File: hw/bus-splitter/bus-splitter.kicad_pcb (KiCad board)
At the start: 2 copper layers, 93 x 22 mm, 29 parts, among them J1 WAGO 243-723, J2 WAGO 243-724, J3 WAGO 243-721, J4 WAGO 243-722, J5 CONN-ISP-6, J6 WAGO 243-723, J7 WAGO 243-724, J8 WAGO 243-721, J9 WAGO 243-722, U1 AM1S-2405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

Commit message: Feat: Finished PCB for review
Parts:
- added LOGO1: OPEN_HARDWARE_1, Symbol:Symbol_OSHW-Logo_Copper, F.Cu at (127.0, 88.0)
- D2: value D -> 1N4148
- F1: value FUSE -> 0,15A
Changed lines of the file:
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@@
     (tracks 156)
     (zones 0)
-    (modules 29)
+    (modules 30)
     (nets 21)
   )
@@
   (title_block
     (title bus-splitter)
-    (date 2018-06-13)
+    (date 2018-06-14)
     (rev 1)
     (company koewiba)
@@
       (effects (font (size 0.8 0.8) (thickness 0.15)) (justify mirror))
     )
-    (fp_text value D (at 0 -1.524 90) (layer B.Fab)
+    (fp_text value 1N4148 (at 0 -1.524 90) (layer B.Fab)
       (effects (font (size 0.8 0.8) (thickness 0.15)) (justify mirror))
     )
@@
       (effects (font (size 0.8 0.8) (thickness 0.15)) (justify mirror))
     )
-    (fp_text value FUSE (at -0.127 -1.905 90) (layer B.Fab)
+    (fp_text value 0,15A (at -0.127 -1.905 90) (layer B.Fab)
       (effects (font (size 0.8 0.8) (thickness 0.15)) (justify mirror))
     )
@@
     )
   )
+  (module Symbol:Symbol_OSHW-Logo_Copper (layer F.Cu)
+    (at 127 88)
+    (descr "Symbol, OSHW-Logo, Copper,")
+    (tags "Symbol, OSHW-Logo, Copper,")
+    (fp_text reference LOGO1 (at 0.09906 -4.38912) (layer F.SilkS) hide
+      (effects (font (size 1 1) (thickness 0.2)))
+    )
+    (fp_text value OPEN_HARDWARE_1 (at 0.30988 6.56082) (layer F.Fab) hide
+      (effects (font (size 1 1) (thickness 0.2)))
+    )
+    (fp_line (start 1.66878 2.68986) (end 2.02946 4.16052) (layer F.Cu) (width 0.381))
+    (fp_line (start 2.02946 4.16052) (end 2.30886 3.0988) (layer F.Cu) (width 0.381))
+    (fp_line (start 2.30886 3.0988) (end 2.61874 4.17068) (layer F.Cu) (width 0.381))
+    (fp_line (start 2.61874 4.17068) (end 2.9591 2.72034) (layer F.Cu) (width 0.381))
+    (fp_line (start 0.24892 3.38074) (end 1.03886 3.37058) (layer F.Cu) (width 0.381))
+    (fp_line (start 1.03886 3.37058) (end 1.04902 3.38074) (layer F.Cu) (width 0.381))
+    (fp_line (start 1.04902 3.38074) (end 1.04902 3.37058) (layer F.Cu) (width 0.381))
+    (fp_line (start 1.08966 2.65938) (end 1.08966 4.20116) (layer F.Cu) (width 0.381))
+    (fp_line (start 0.20066 2.64922) (end 0.20066 4.21894) (layer F.Cu) (width 0.381))
+    (fp_line (start 0.20066 4.21894) (end 0.21082 4.20878) (layer F.Cu) (width 0.381))
+    (fp_line (start -0.35052 2.75082) (end -0.70104 2.66954) (layer F.Cu) (width 0.381))
+    (fp_line (start -0.70104 2.66954) (end -1.02108 2.65938) (layer F.Cu) (width 0.381))
+    (fp_line (start -1.02108 2.65938) (end -1.25984 2.86004) (layer F.Cu) (width 0.381))
+    (fp_line (start -1.25984 2.86004) (end -1.29032 3.12928) (layer F.Cu) (width 0.381))
+    (fp_line (start -1.29032 3.12928) (end -1.04902 3.37058) (layer F.Cu) (width 0.381))
+    (fp_line (start -1.04902 3.37058) (end -0.6604 3.50012) (layer F.Cu) (width 0.381))
+    (fp_line (start -0.6604 3.50012) (end -0.48006 3.66014) (layer F.Cu) (width 0.381))
+    (fp_line (start -0.48006 3.66014) (end -0.43942 3.95986) (layer F.Cu) (width 0.381))
+    (fp_line (start -0.43942 3.95986) (end -0.67056 4.18084) (layer F.Cu) (width 0.381))
+    (fp_line (start -0.67056 4.18084) (end -0.9906 4.20878) (layer F.Cu) (width 0.381))
+    (fp_line (start -0.9906 4.20878) (end -1.34112 4.09956) (layer F.Cu) (width 0.381))
+    (fp_line (start -2.37998 2.64922) (end -2.6289 2.66954) (layer F.Cu) (width 0.381))
+    (fp_line (start -2.6289 2.66954) (end -2.8702 2.91084) (layer F.Cu) (width 0.381))
+    (fp_line (start -2.8702 2.91084) (end -2.9591 3.40106) (layer F.Cu) (width 0.381))
+    (fp_line (start -2.9591 3.40106) (end -2.93116 3.74904) (layer F.Cu) (width 0.381))
+    (fp_line (start -2.93116 3.74904) (end -2.7305 4.06908) (layer F.Cu) (width 0.381))
+    (fp_line (start -2.7305 4.06908) (end -2.47904 4.191) (layer F.Cu) (width 0.381))
+    (fp_line (start -2.47904 4.191) (end -2.16916 4.11988) (layer F.Cu) (width 0.381))
+    (fp_line (start -2.16916 4.11988) (end -1.95072 3.93954) (layer F.Cu) (width 0.381))
+    (fp_line (start -1.95072 3.93954) (end -1.8796 3.4798) (layer F.Cu) (width 0.381))
+    (fp_line (start -1.8796 3.4798) (end -1.9304 3.07086) (layer F.Cu) (width 0.381))
+    (fp_line (start -1.9304 3.07086) (end -2.03962 2.78892) (layer F.Cu) (width 0.381))
+    (fp_line (start -2.03962 2.78892) (end -2.4003 2.65938) (layer F.Cu) (width 0.381))
+    (fp_line (start -1.78054 0.92964) (end -2.03962 1.49098) (layer F.Cu) (width 0.381))
+    (fp_line (start -2.03962 1.49098) (end -1.50114 2.00914) (layer F.Cu) (width 0.381))
+    (fp_line (start -1.50114 2.00914) (end -0.98044 1.7399) (layer F.Cu) (width 0.381))
+    (fp_line (start -0.98044 1.7399) (end -0.70104 1.89992) (layer F.Cu) (width 0.381))
+    (fp_line (start 0.73914 1.8796) (end 1.06934 1.6891) (layer F.Cu) (width 0.381))
+    (fp_line (start 1.06934 1.6891) (end 1.50876 2.0193) (layer F.Cu) (width 0.381))
+    (fp_line (start 1.50876 2.0193) (end 1.9812 1.52908) (layer F.Cu) (width 0.381))
+    (fp_line (start 1.9812 1.52908) (end 1.69926 1.04902) (layer F.Cu) (width 0.381))
+    (fp_line (start 1.69926 1.04902) (end 1.88976 0.57912) (layer F.Cu) (width 0.381))
+    (fp_line (start 1.88976 0.57912) (end 2.49936 0.39116) (layer F.Cu) (width 0.381))
+    (fp_line (start 2.49936 0.39116) (end 2.49936 -0.28956) (layer F.Cu) (width 0.381))
+    (fp_line (start 2.49936 -0.28956) (end 1.94056 -0.42926) (layer F.Cu) (width 0.381))
+    (fp_line (start 1.94056 -0.42926) (end 1.7399 -1.00076) (layer F.Cu) (width 0.381))
+    (fp_line (start 1.7399 -1.00076) (end 2.00914 -1.47066) (layer F.Cu) (width 0.381))
+    (fp_line (start 2.00914 -1.47066) (end 1.53924 -1.9812) (layer F.Cu) (width 0.381))
+    (fp_line (start 1.53924 -1.9812) (end 1.02108 -1.71958) (layer F.Cu) (width 0.381))
+    (fp_line (start 1.02108 -1.71958) (end 0.55118 -1.92024) (layer F.Cu) (width 0.381))
+    (fp_line (start 0.55118 -1.92024) (end 0.381 -2.46126) (layer F.Cu) (width 0.381))
+    (fp_line (start 0.381 -2.46126) (end -0.30988 -2.47904) (layer F.Cu) (width 0.381))
+    (fp_line (start -0.30988 -2.47904) (end -0.5207 -1.9304) (layer F.Cu) (width 0.381))
+    (fp_line (start -0.5207 -1.9304) (end -0.9398 -1.76022) (layer F.Cu) (width 0.381))
+    (fp_line (start -0.9398 -1.76022) (end -1.49098 -2.02946) (layer F.Cu) (width 0.381))
+    (fp_line (start -1.49098 -2.02946) (end -2.00914 -1.50114) (layer F.Cu) (width 0.381))
+    (fp_line (start -2.00914 -1.50114) (end -1.76022 -0.96012) (layer F.Cu) (width 0.381))
+    (fp_line (start -1.76022 -0.96012) (end -1.9304 -0.48006) (layer F.Cu) (width 0.381))
+    (fp_line (start -1.9304 -0.48006) (end -2.47904 -0.381) (layer F.Cu) (width 0.381))
+    (fp_line (start -2.47904 -0.381) (end -2.4892 0.32004) (layer F.Cu) (width 0.381))
+    (fp_line (start -2.4892 0.32004) (end -1.9304 0.5207) (layer F.Cu) (width 0.381))
+    (fp_line (start -1.9304 0.5207) (end -1.7907 0.91948) (layer F.Cu) (width 0.381))
+    (fp_line (start 0.35052 0.89916) (end 0.65024 0.7493) (layer F.Cu) (width 0.381))
+    (fp_line (start 0.65024 0.7493) (end 0.8509 0.55118) (layer F.Cu) (width 0.381))
+    (fp_line (start 0.8509 0.55118) (end 1.00076 0.14986) (layer F.Cu) (width 0.381))
+    (fp_line (start 1.00076 0.14986) (end 1.00076 -0.24892) (layer F.Cu) (width 0.381))
+    (fp_line (start 1.00076 -0.24892) (end 0.8509 -0.59944) (layer F.Cu) (width 0.381))
+    (fp_line (start 0.8509 -0.59944) (end 0.39878 -0.94996) (layer F.Cu) (width 0.381))
+    (fp_line (start 0.39878 -0.94996) (end -0.0508 -1.00076) (layer F.Cu) (width 0.381))
+    (fp_line (start -0.0508 -1.00076) (end -0.44958 -0.89916) (layer F.Cu) (width 0.381))
+    (fp_line (start -0.44958 -0.89916) (end -0.8509 -0.55118) (layer F.Cu) (width 0.381))
+    (fp_line (start -0.8509 -0.55118) (end -1.00076 -0.09906) (layer F.Cu) (width 0.381))
+    (fp_line (start -1.00076 -0.09906) (end -0.94996 0.39878) (layer F.Cu) (width 0.381))
+    (fp_line (start -0.94996 0.39878) (end -0.70104 0.70104) (layer F.Cu) (width 0.381))
+    (fp_line (start -0.70104 0.70104) (end -0.35052 0.89916) (layer F.Cu) (width 0.381))
+    (fp_line (start -0.35052 0.89916) (end -0.70104 1.89992) (layer F.Cu) (width 0.381))
+    (fp_line (start 0.35052 0.89916) (end 0.7493 1.89992) (layer F.Cu) (width 0.381))
+  )
   (gr_text "bus-splitter Rev 1\nkoewiba" (at 177.8 76.835) (layer B.Cu)

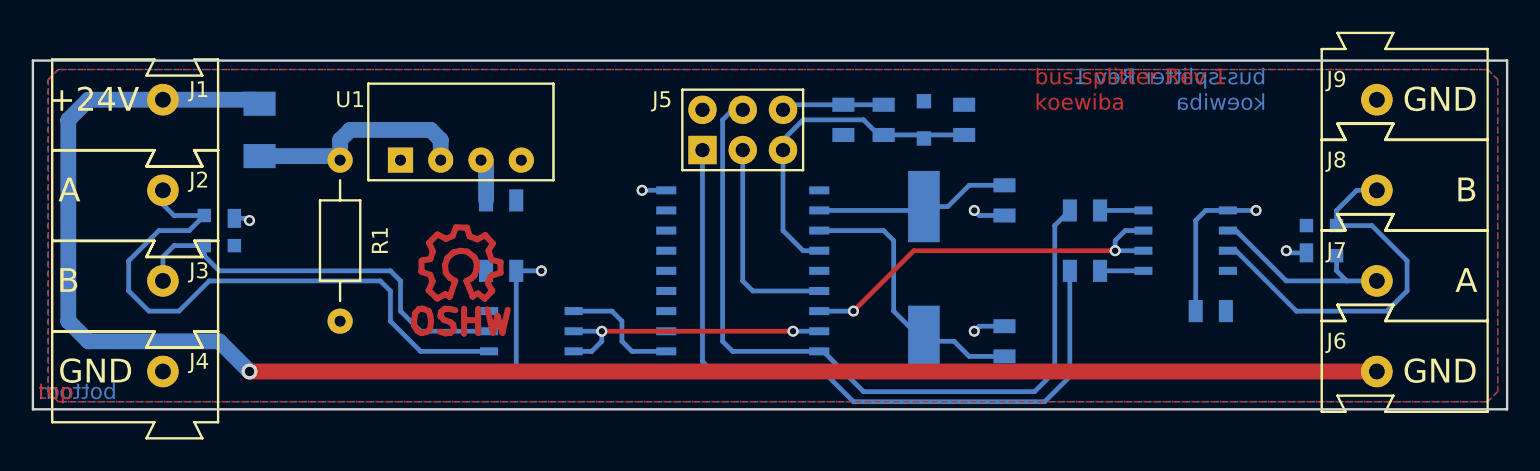
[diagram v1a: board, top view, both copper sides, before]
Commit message: added testpoints
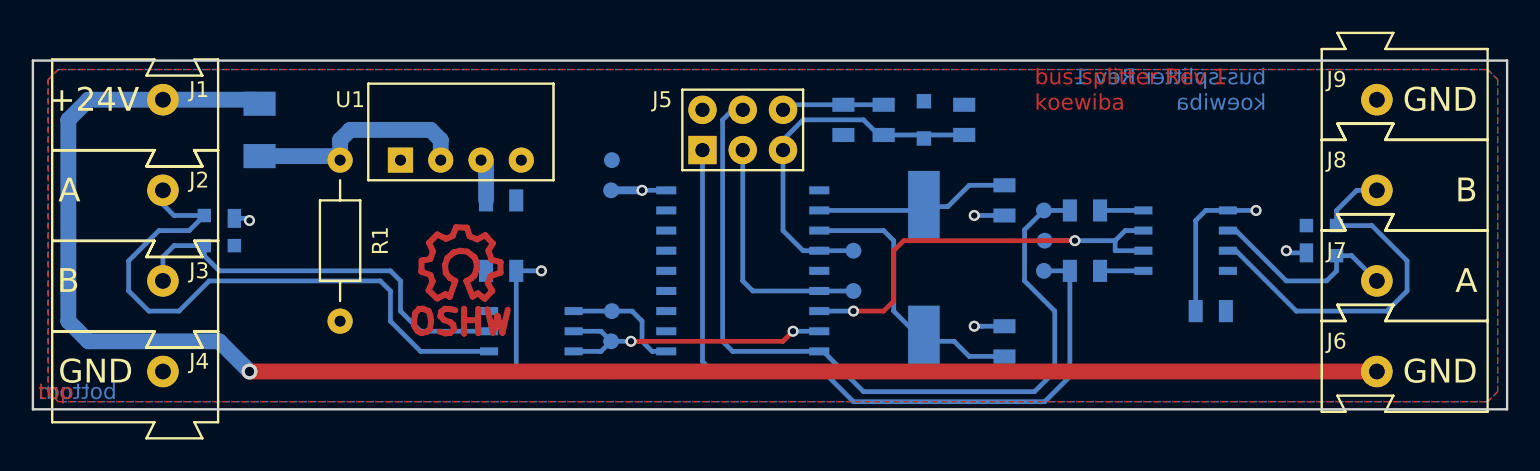
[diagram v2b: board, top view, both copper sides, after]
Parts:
- added J10: tp_vcc, Connector_Miscelleaneus:Testpoint_1mm, B.Cu at (136.6, 81.3)
- added J11: tp_gnd, Connector_Miscelleaneus:Testpoint_1mm, B.Cu at (136.5, 83.2)
- added J12: tp_txd0, Connector_Miscelleaneus:Testpoint_1mm, B.Cu at (136.5, 94.6)
- added J13: tp_rxd0, Connector_Miscelleaneus:Testpoint_1mm, B.Cu at (136.6, 90.8)
- added J14: tp_txden0, Connector_Miscelleaneus:Testpoint_1mm, B.Cu at (136.5, 92.7)
- added J15: tp_reset, Connector_Miscelleaneus:Testpoint_1mm, B.Cu at (151.8, 87.0)
- added J16: tp_txd1_mosi, Connector_Miscelleaneus:Testpoint_1mm, B.Cu at (163.8, 84.5)
- added J17: tp_rxd1_miso, Connector_Miscelleaneus:Testpoint_1mm, B.Cu at (163.8, 88.3)
- added J18: tp_sck, Connector_Miscelleaneus:Testpoint_1mm, B.Cu at (151.8, 89.5)
- added J19: tp_txden1, Connector_Miscelleaneus:Testpoint_1mm, B.Cu at (163.9, 86.4)
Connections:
- D1 pad 2: (no net) -> Net-(D1-Pad2)
- D3 pad 2: (no net) -> Net-(D3-Pad2)
- U4 pad 15: (no net) -> Net-(U4-Pad15)
- U4 pad 3: (no net) -> Net-(U4-Pad3)
- U4 pad 4: (no net) -> Net-(U4-Pad4)
- U4 pad 5: (no net) -> Net-(U4-Pad5)
- U4 pad 6: (no net) -> Net-(U4-Pad6)
- U4 pad 7: (no net) -> Net-(U4-Pad7)
- U4 pad 8: (no net) -> Net-(U4-Pad8)
- U4 pad 9: (no net) -> Net-(U4-Pad9)
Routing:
- net /TXDEN1: track 24.7 -> 28.7 mm
- net /TXD1_MOSI: track 49.1 -> 51.7 mm
- net /SCK: track 14.0 -> 16.1 mm
- net //RESET: track 21.1 -> 23.2 mm
- net GND: track 36.3 -> 38.0 mm
- net /RXD1_MISO: track 45.5 -> 47.2 mm
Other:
- net class Power: trace_width 1 -> 0.5

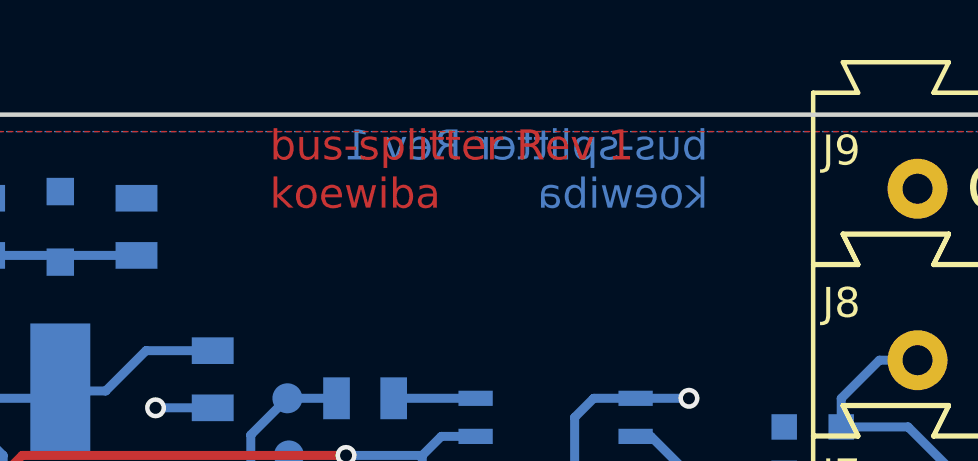
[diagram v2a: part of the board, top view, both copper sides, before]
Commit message: Added 3d images Added component placement drawings Added gerber files Fixes rescue library mess
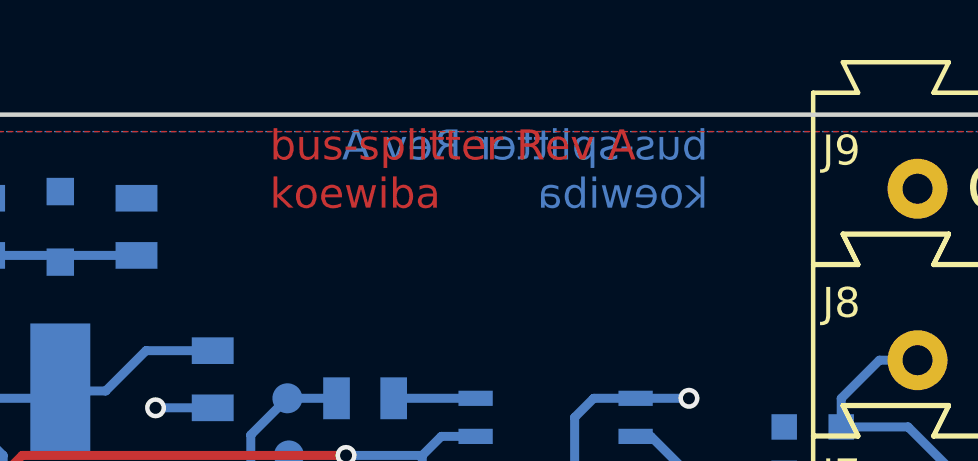
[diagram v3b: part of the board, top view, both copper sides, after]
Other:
- board text added: "bus-splitter Rev A koewiba"
- board text removed: "bus-splitter Rev 1 koewiba"
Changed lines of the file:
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@@
-(kicad_pcb (version 20171130) (host pcbnew 5.0.0-fee4fd1~66~ubuntu18.04.1)
+(kicad_pcb (version 20171130) (host pcbnew 5.0.0-fee4fd1~66~ubuntu16.04.1)
   (general
     (thickness 1.6)
@@
   (title_block
     (title bus-splitter)
-    (date 2018-06-14)
-    (rev 1)
+    (date 2018-09-26)
+    (rev A)
     (company koewiba)
   )
@@
     (visible_elements 7FFFFFFF)
     (pcbplotparams
-      (layerselection 0x00030_80000001)
+      (layerselection 0x013b0_ffffffff)
       (usegerberextensions false)
       (usegerberattributes false)
@@
       (outputformat 1)
       (mirror false)
-      (drillshape 1)
+      (drillshape 0)
       (scaleselection 1)
-      (outputdirectory ""))
+      (outputdirectory "gerber"))
   )
   (net 0 "")
@@
       (net 16 /TXDEN1))
   )
-  (gr_text "bus-splitter Rev 1\nkoewiba" (at 177.8 76.835) (layer B.Cu)
+  (gr_text "bus-splitter Rev A\nkoewiba" (at 177.8 76.835) (layer B.Cu)
     (effects (font (size 1 1) (thickness 0.2)) (justify left mirror))
   )
-  (gr_text "bus-splitter Rev 1\nkoewiba" (at 163.195 76.835) (layer F.Cu)
+  (gr_text "bus-splitter Rev A\nkoewiba" (at 163.195 76.835) (layer F.Cu)
     (effects (font (size 1 1) (thickness 0.2)) (justify left))
   )
